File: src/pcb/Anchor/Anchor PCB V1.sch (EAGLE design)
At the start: 85 parts, among them IC1 ENC28J60-I_SS, IC2 TPS23750PWP, IC3 MIC5219-3.3YM5-TR, IC4 DWM1000, J1 0826-1X1T-GJ-F, J2 105017-0001, Q1 32 MHz, Q2 SUD06N10-225L, U1 ATSAMD21G-A, Y1 25 MHz

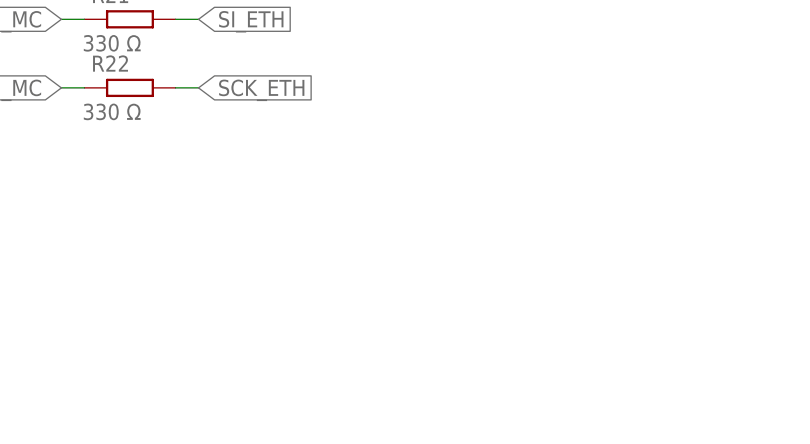
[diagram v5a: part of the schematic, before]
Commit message: Added mounting holes
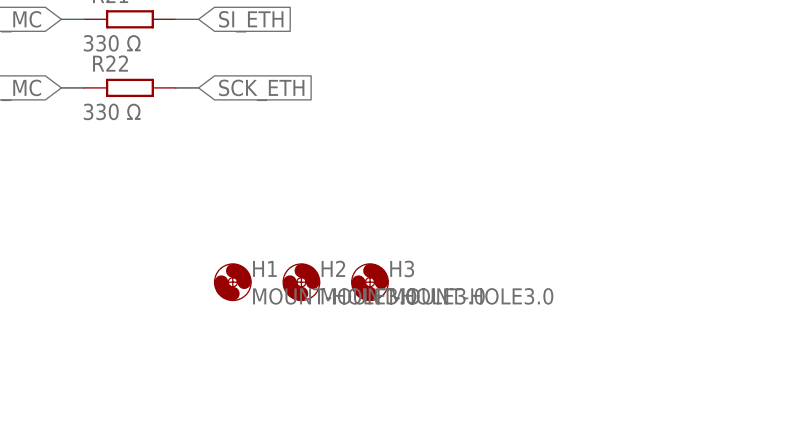
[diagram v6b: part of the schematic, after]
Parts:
- added H1, H2, H3: MOUNT-HOLE3.0, holes:MOUNT-HOLE3.0
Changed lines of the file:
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@@
 <part name="C24" library="rcl" library_urn="urn:adsk.eagle:library:334" deviceset="C-EU" device="C0805" package3d_urn="urn:adsk.eagle:package:23617/2" value="2.2 µF"/>
 <part name="P+17" library="supply1" library_urn="urn:adsk.eagle:library:371" deviceset="VCC" device="" value="3.3V"/>
+<part name="H1" library="holes" library_urn="urn:adsk.eagle:library:237" deviceset="MOUNT-HOLE" device="3.0" package3d_urn="urn:adsk.eagle:package:14277/1"/>
+<part name="H2" library="holes" library_urn="urn:adsk.eagle:library:237" deviceset="MOUNT-HOLE" device="3.0" package3d_urn="urn:adsk.eagle:package:14277/1"/>
+<part name="H3" library="holes" library_urn="urn:adsk.eagle:library:237" deviceset="MOUNT-HOLE" device="3.0" package3d_urn="urn:adsk.eagle:package:14277/1"/>
 </parts>
 <sheets>
@@
 <attribute name="VALUE" x="-307.34" y="113.03" size="1.778" layer="96" rot="R180"/>
 </instance>
+<instance part="H1" gate="G$1" x="-640.08" y="-45.72" smashed="yes">
+<attribute name="NAME" x="-638.048" y="-45.1358" size="1.778" layer="95"/>
+<attribute name="VALUE" x="-638.048" y="-48.1838" size="1.778" layer="96"/>
+</instance>
+<instance part="H2" gate="G$1" x="-632.46" y="-45.72" smashed="yes">
+<attribute name="NAME" x="-630.428" y="-45.1358" size="1.778" layer="95"/>
+<attribute name="VALUE" x="-630.428" y="-48.1838" size="1.778" layer="96"/>
+</instance>
+<instance part="H3" gate="G$1" x="-624.84" y="-45.72" smashed="yes">
+<attribute name="NAME" x="-622.808" y="-45.1358" size="1.778" layer="95"/>
+<attribute name="VALUE" x="-622.808" y="-48.1838" size="1.778" layer="96"/>
+</instance>
 </instances>
